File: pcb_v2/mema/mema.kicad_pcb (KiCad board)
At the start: 2 copper layers, 137.8 x 70.5 mm, 21 parts, among them J1 bus_mem_1, J2 bus_mem_2, J3 cartridge, U1 CY62256-70PC, U2 CY62256-70PC, U3 74LS283, U4 74LS00, U5 74LS32, U7 74LS138

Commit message: roteamento com problemas; refazer
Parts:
- moved R4 19.3 mm to (78.1, 87.0), turned to -90 degrees
- moved R3 15.2 mm to (74.1, 87.0), turned to -90 degrees
- moved R1 10.9 mm to (74.1, 104.8), turned to 90 degrees
- moved R2 7.21 mm to (78.1, 104.8), turned to 90 degrees
- moved U7 2.54 mm to (144.8, 105.4)
- moved C4 1.91 mm to (143.5, 83.7)
- moved C5 1.91 mm to (143.5, 64.1)
- moved J2 1.91 mm to (92.1, 52.1)
- moved U3 1.91 mm to (61.0, 86.4)
- moved D5 1.75 mm to (122.6, 55.9), turned to 90 degrees
- moved C3 1.42 mm to (63.6, 82.5)
- moved C1 1.27 mm to (101.7, 68.6)
- moved C2 1.27 mm to (127.7, 68.6)
- moved C7 0.63 mm to (141.0, 102.8)
- moved U5 0.63 mm to (147.3, 66.7)
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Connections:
- J3 pad 3: ~{rom_select} -> rom_select
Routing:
- net +5V: track 0.00 -> 242.9 mm
- net rom_select: track 0.00 -> 140.9 mm, vias 0 -> 2
- net data_{3}: track 0.00 -> 137.1 mm, vias 0 -> 2
- net data_{4}: track 0.00 -> 134.9 mm, vias 0 -> 2
- net data_{7}: track 0.00 -> 134.6 mm, vias 0 -> 2
- net data_{5}: track 0.00 -> 134.2 mm, vias 0 -> 2
- net data_{6}: track 0.00 -> 134.1 mm, vias 0 -> 2
- net addr_{0}: track 0.00 -> 129.1 mm, vias 0 -> 2
- net addr_{1}: track 0.00 -> 125.8 mm, vias 0 -> 2
- net addr_{2}: track 0.00 -> 125.7 mm, vias 0 -> 2
- net addr_{4}: track 0.00 -> 122.3 mm, vias 0 -> 1
- net addr_{3}: track 0.00 -> 120.5 mm, vias 0 -> 1
- net data_{2}: track 0.00 -> 118.8 mm, vias 0 -> 1
- net data_{0}: track 0.00 -> 117.2 mm, vias 0 -> 1
- net data_{1}: track 0.00 -> 115.7 mm, vias 0 -> 1
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- added copper zone on B.Cu, net GND
- added copper zone on F.Cu, net GND

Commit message: concluído o roteamento
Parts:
- J1: value bus_mem_1 -> bus mem 1
- J2: value bus_mem_2 -> bus mem 2
- moved R5 31.3 mm to (151.1, 53.3), turned to 180 degrees
- moved D5 25.9 mm to (147.3, 48.3), turned to 0 degrees
- moved R2 17.8 mm to (78.1, 87.0), turned to -90 degrees
- moved R4 17.8 mm to (78.1, 104.8), turned to 90 degrees
- moved C7 10.8 mm to (141.0, 92.0)
- moved U7 10.8 mm to (144.8, 94.6)
- moved U4 5.72 mm to (147.3, 80.6)
- moved C4 5.71 mm to (143.5, 78.0)
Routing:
- net addr_{15}: track 27.5 -> 193.1 mm, vias 0 -> 2
- net ~{memory_read}: track 18.2 -> 156.4 mm, vias 1 -> 2
- net memory_read: track 27.1 -> 150.4 mm, vias 0 -> 1
- net addr_{12}: track 52.9 -> 165.2 mm, vias 1 -> 3
- net addr_{11}: track 44.8 -> 151.8 mm, vias 1 -> 2
- net memory_write: track 0.00 -> 103.5 mm
- net addr_{9}: track 44.8 -> 146.4 mm, vias 1 -> 3
- net clock: track 0.00 -> 101.2 mm, vias 0 -> 1
- net addr_{8}: track 44.8 -> 142.7 mm, vias 1 -> 3
- net addr_{6}: track 27.1 -> 125.0 mm, vias 0 -> 3
- net addr_{14}: track 56.7 -> 153.5 mm, vias 0 -> 4
- net ~{write_enable}: track 45.4 -> 141.7 mm, vias 1 -> 0
- net addr_{7}: track 27.1 -> 123.3 mm, vias 0 -> 3
- net addr_{13}: track 65.7 -> 155.9 mm, vias 1 -> 4
- net rom_address: track 0.00 -> 84.5 mm, vias 0 -> 1
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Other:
- board size 137.8 x 70.5 mm -> 142.2 x 70.5 mm

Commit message: concluído o roteamento
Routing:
- net addr_{10}: track 158.8 -> 155.8 mm
- net memory_read: track 150.4 -> 148.9 mm
- net +5V: track 270.4 -> 271.2 mm
- net addr_{2}: track 125.4 -> 124.7 mm
- net GND: vias 2 -> 4

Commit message: experimentação com opcodes
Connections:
- J1 pad 11: data_{5} -> data_{2}
- J1 pad 13: data_{6} -> data_{1}
- J1 pad 14: data_{7} -> data_{0}
- J1 pad 3: data_{1} -> data_{6}
- J1 pad 4: data_{0} -> data_{7}
- J1 pad 5: data_{2} -> data_{5}
- J1 pad 7: data_{3} -> data_{4}
- J1 pad 9: data_{4} -> data_{3}
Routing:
- net data_{0}: track 115.5 -> 121.2 mm, vias 2 -> 1
- net data_{2}: track 118.7 -> 116.3 mm, vias 2 -> 1
- net data_{3}: track 136.8 -> 134.9 mm, vias 2 -> 1
- net data_{4}: track 137.0 -> 135.1 mm
- net data_{5}: track 136.5 -> 135.2 mm
- net data_{1}: track 114.7 -> 114.6 mm, vias 2 -> 1

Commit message: redimensionamento do pcb e início do layout
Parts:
- moved J1 151.6 mm to (122.6, 191.1)
- moved J3 133.4 mm to (47.6, 184.2), turned to 90 degrees
- moved J2 130.0 mm to (122.6, 178.4)
- moved U7 99.0 mm to (48.9, 69.8), turned to 0 degrees
- moved D5 96.0 mm to (51.4, 53.3)
- moved C7 93.1 mm to (51.5, 66.0), turned to 0 degrees
- moved R5 92.8 mm to (58.4, 48.3), turned to -90 degrees
- moved U4 82.6 mm to (65.4, 69.8), turned to 0 degrees
- moved C4 76.4 mm to (68.0, 66.0), turned to 0 degrees
- moved R3 69.8 mm to (114.3, 144.0), turned to 0 degrees
- moved R2 64.1 mm to (114.3, 139.9), turned to 0 degrees
- moved C1 58.0 mm to (59.1, 108.0)
- moved U1 58.0 mm to (48.9, 111.8)
- moved R1 57.1 mm to (121.9, 135.9), turned to 180 degrees
- moved C2 53.9 mm to (90.9, 108.0)
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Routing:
- net +5V: track 271.2 -> 0.00 mm
- net addr_{15}: track 193.1 -> 0.00 mm, vias 2 -> 0
- net addr_{12}: track 165.2 -> 0.00 mm, vias 3 -> 0
- net rom_select: track 163.8 -> 0.00 mm, vias 2 -> 0
- net ~{memory_read}: track 156.4 -> 0.00 mm, vias 2 -> 0
- net addr_{13}: track 155.9 -> 0.00 mm, vias 4 -> 0
- net addr_{10}: track 155.8 -> 0.00 mm, vias 2 -> 0
- net addr_{14}: track 153.5 -> 0.00 mm, vias 4 -> 0
- net addr_{11}: track 151.8 -> 0.00 mm, vias 2 -> 0
- net memory_read: track 148.9 -> 0.00 mm, vias 1 -> 0
- net addr_{9}: track 146.4 -> 0.00 mm, vias 3 -> 0
- net addr_{8}: track 142.7 -> 0.00 mm, vias 3 -> 0
- net ~{write_enable}: track 141.7 -> 0.00 mm
- net addr_{4}: track 125.3 -> 0.00 mm, vias 2 -> 0
- net addr_{6}: track 125.0 -> 0.00 mm, vias 3 -> 0
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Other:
- board size 142.2 x 70.5 mm -> 114.9 x 165 mm

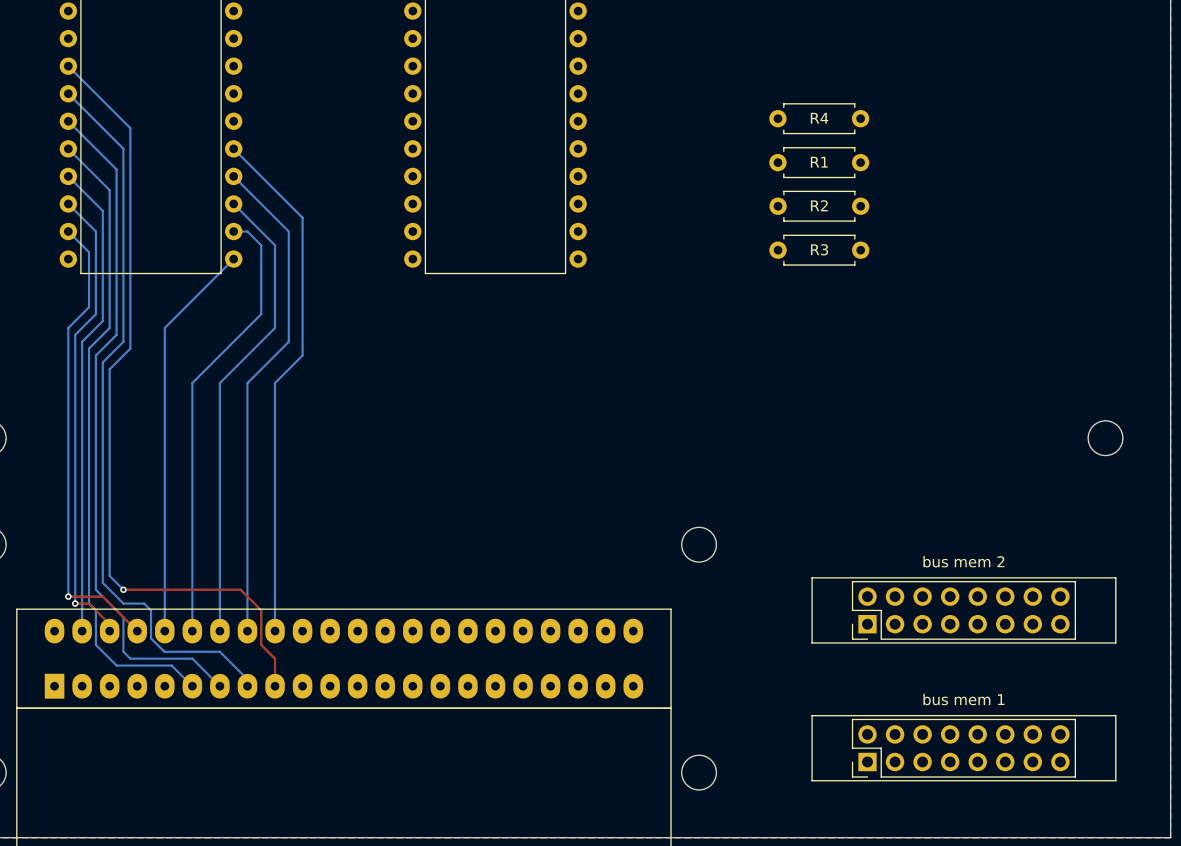
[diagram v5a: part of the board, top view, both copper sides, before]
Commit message: layout do pcb já considerando as dimensões corretas
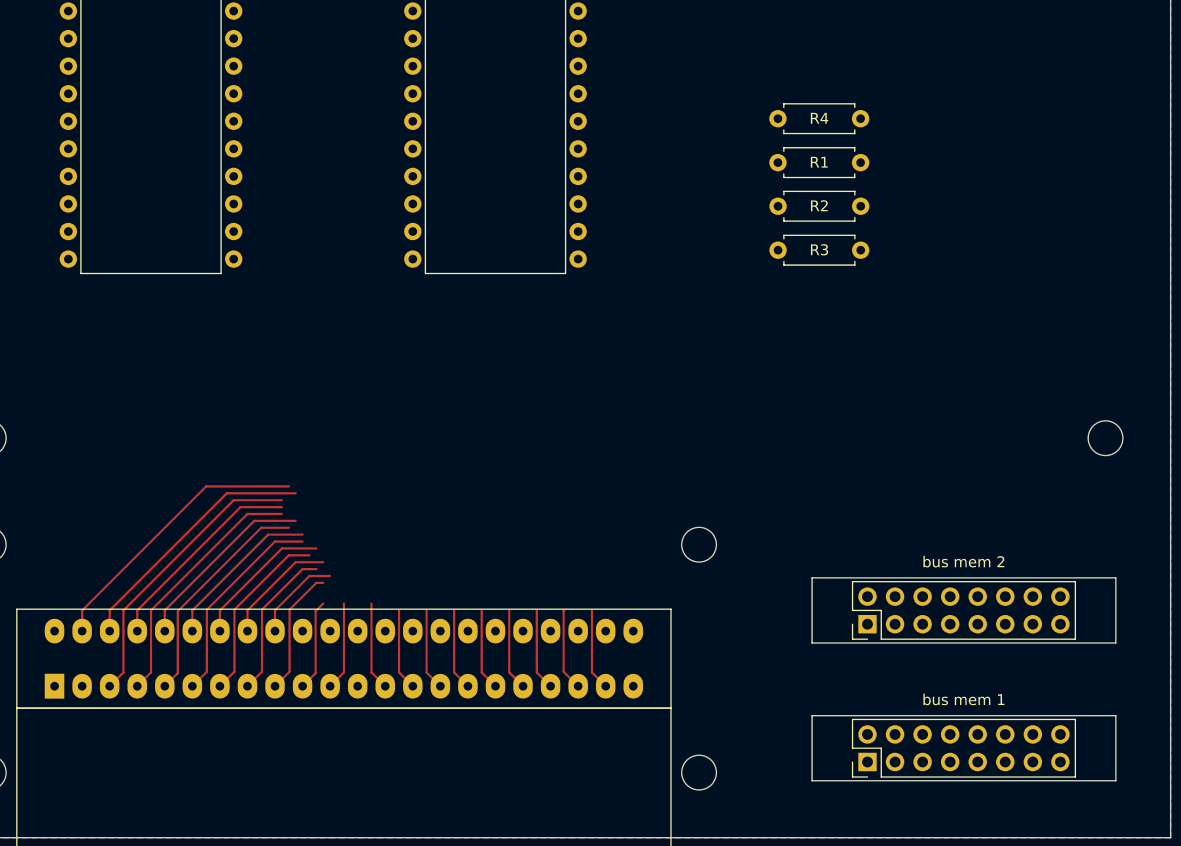
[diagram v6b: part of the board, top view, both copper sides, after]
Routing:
- net addr_{3}: track 72.9 -> 11.7 mm, vias 1 -> 0
- net addr_{2}: track 67.1 -> 14.2 mm
- net addr_{1}: track 62.8 -> 16.6 mm
- net data_{7}: track 48.1 -> 8.30 mm
- net addr_{0}: track 58.8 -> 19.0 mm
- net data_{6}: track 45.6 -> 10.7 mm
- net data_{5}: track 43.1 -> 13.2 mm
- net rom_select: track 0.00 -> 26.3 mm
- net data_{4}: track 41.3 -> 15.0 mm
- net data_{2}: track 42.9 -> 19.2 mm, vias 1 -> 0
- net ~{write_enable}: track 0.00 -> 23.3 mm
- net ~{memory_read}: track 0.00 -> 20.8 mm
- net data_{1}: track 43.3 -> 23.5 mm, vias 1 -> 0
- net data_{3}: track 36.9 -> 17.4 mm
- net data_{0}: track 44.0 -> 25.7 mm
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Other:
- outline, holes or cut-outs redrawn
